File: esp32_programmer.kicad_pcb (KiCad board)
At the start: 2 copper layers, 29.5 x 25.5 mm, 14 parts, among them J1 MicroQTJ, J2 Conn_01x06_Male, Q1 Q_NPN_BCE, Q2 Q_NPN_BCE, U1 AMS1117-3.3, U2 CH340G, Y1 XSHEELNANF-12MHZ

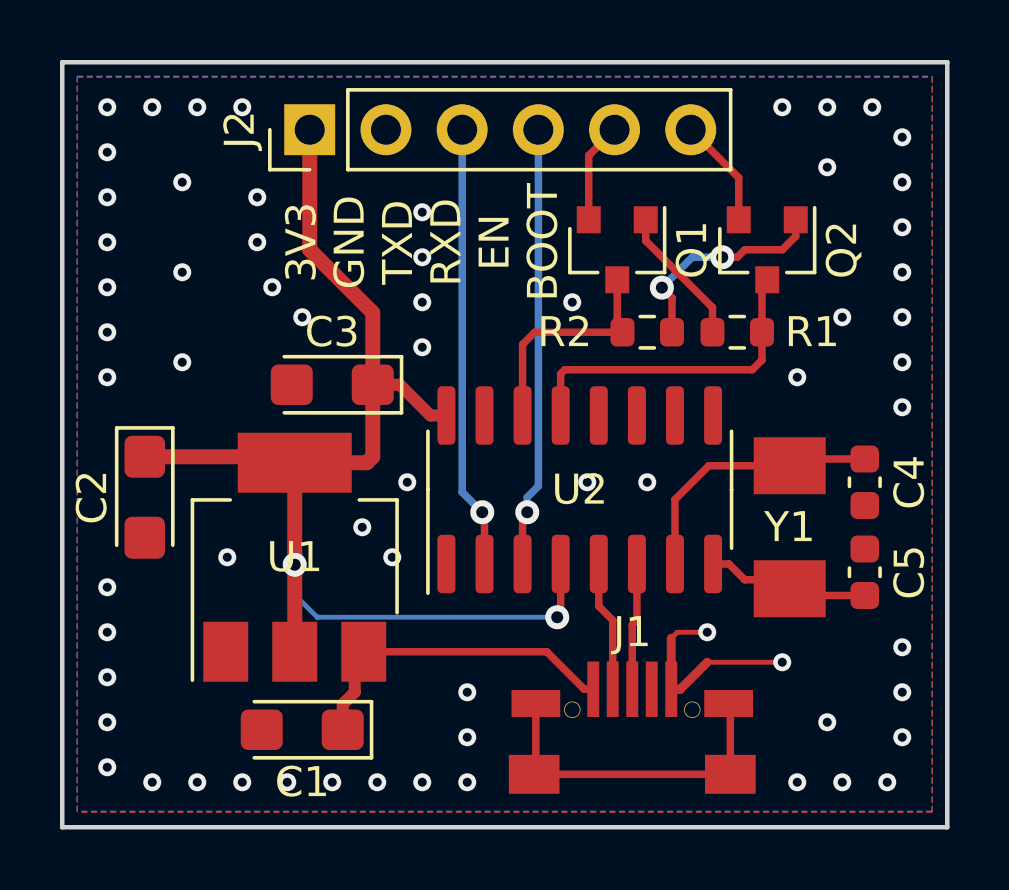
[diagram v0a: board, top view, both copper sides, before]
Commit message: Design review: Modifications made
Thickened power traces to 0.4mm
Changed USB connector footrpint to comply with jlcpcb capabilities.
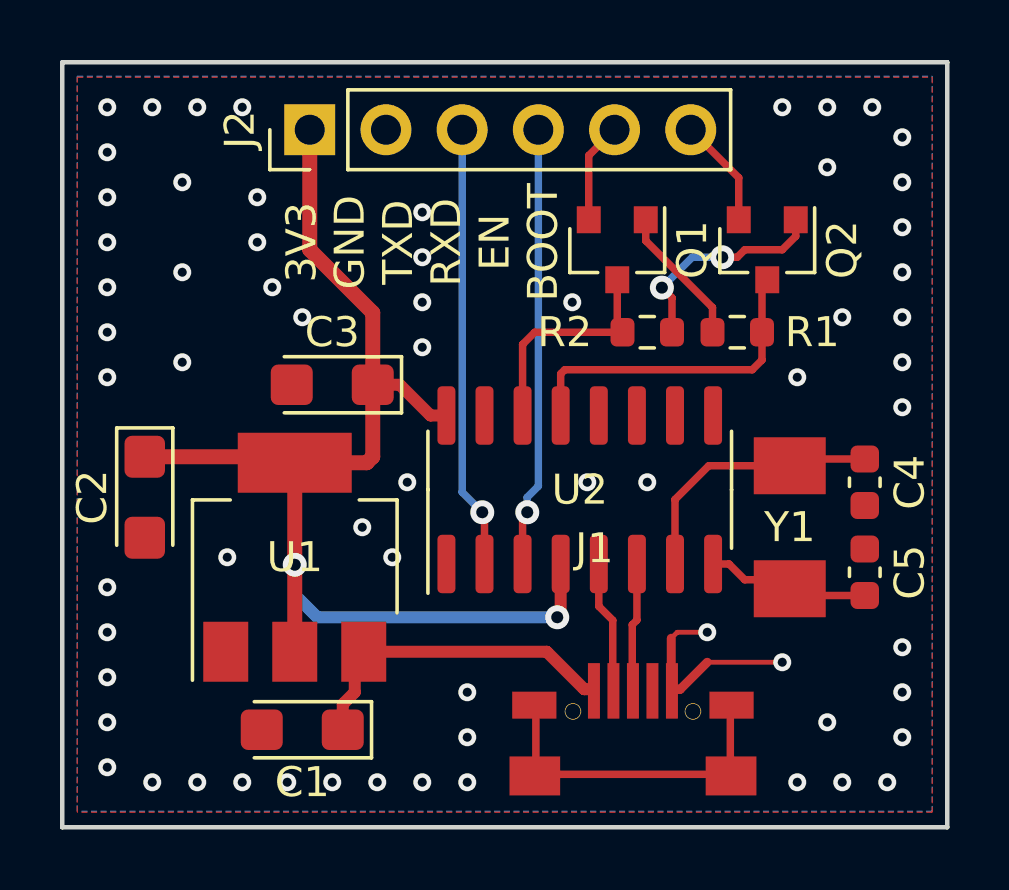
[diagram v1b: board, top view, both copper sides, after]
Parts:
- moved J1 3.07 mm to (129.2, 84.5)
